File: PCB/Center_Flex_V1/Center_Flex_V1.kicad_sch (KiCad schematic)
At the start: 57 parts, among them J1 Conn_01x02_Pin, J10 Conn_01x02_Socket, J11 Conn_01x02_Pin, J12 Conn_01x02_Socket, J13 Conn_01x02_Socket, J14 Conn_01x02_Pin, J15 Conn_01x02_Pin, J16 Conn_01x02_Socket, J17 Conn_01x02_Socket, J18 Conn_01x02_Pin, J19 Conn_01x02_Pin, J2 Conn_01x02_Socket, J20 Conn_01x02_Socket, J21 Conn_01x02_Pin, J22 Conn_01x02_Socket, J23 Conn_01x02_Socket, J24 Conn_01x02_Pin, J25 Conn_01x02_Pin, J26 Conn_01x02_Socket, J27 Conn_01x02_Socket, J28 Conn_01x02_Pin, J29 Conn_01x02_Pin, J3 Conn_01x02_Socket, J30 Conn_01x02_Socket, J31 Conn_01x02_Pin, J32 Conn_01x02_Socket, J33 Conn_01x02_Socket, J34 Conn_01x02_Pin, J35 Conn_01x02_Pin, J36 Conn_01x02_Socket, J37 Conn_01x02_Socket, J38 Conn_01x02_Pin, J39 Conn_01x02_Pin, J4 Conn_01x02_Pin, J40 Conn_01x02_Socket, J5 Conn_01x02_Pin, J6 Conn_01x02_Socket, J7 Conn_01x02_Socket, J8 Conn_01x02_Pin, J9 Conn_01x02_Pin

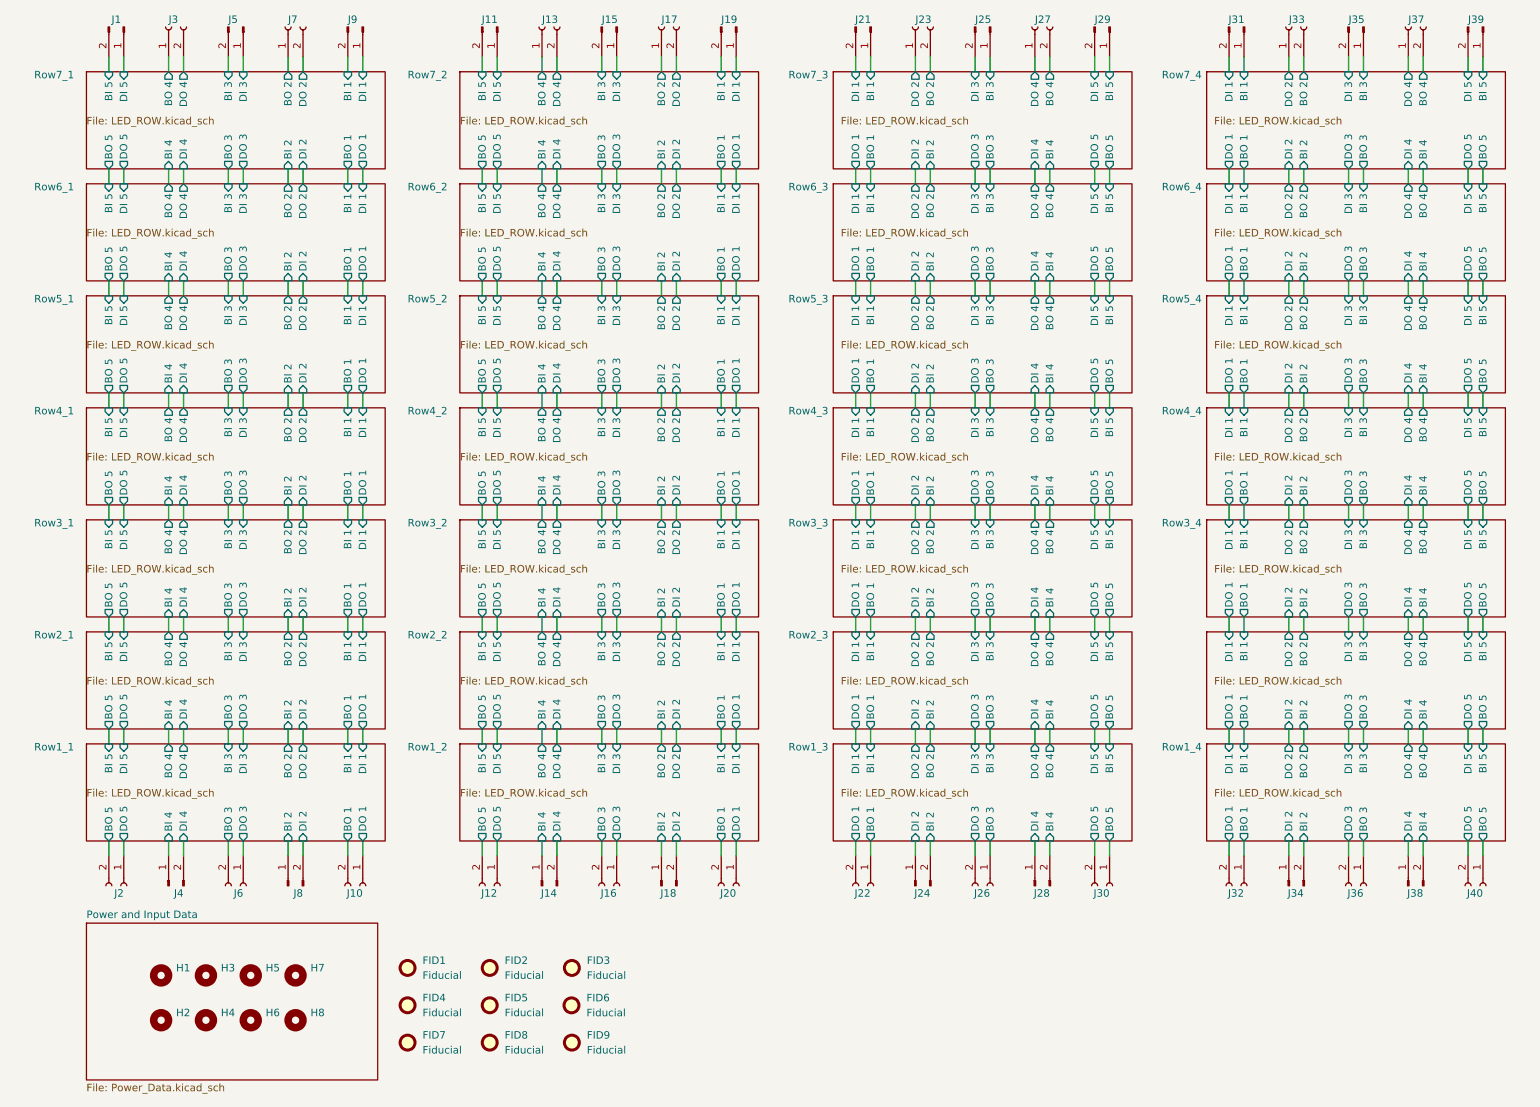
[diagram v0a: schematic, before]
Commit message: Flex PCBs ordered
All Flex PCBs are finalized and ordered
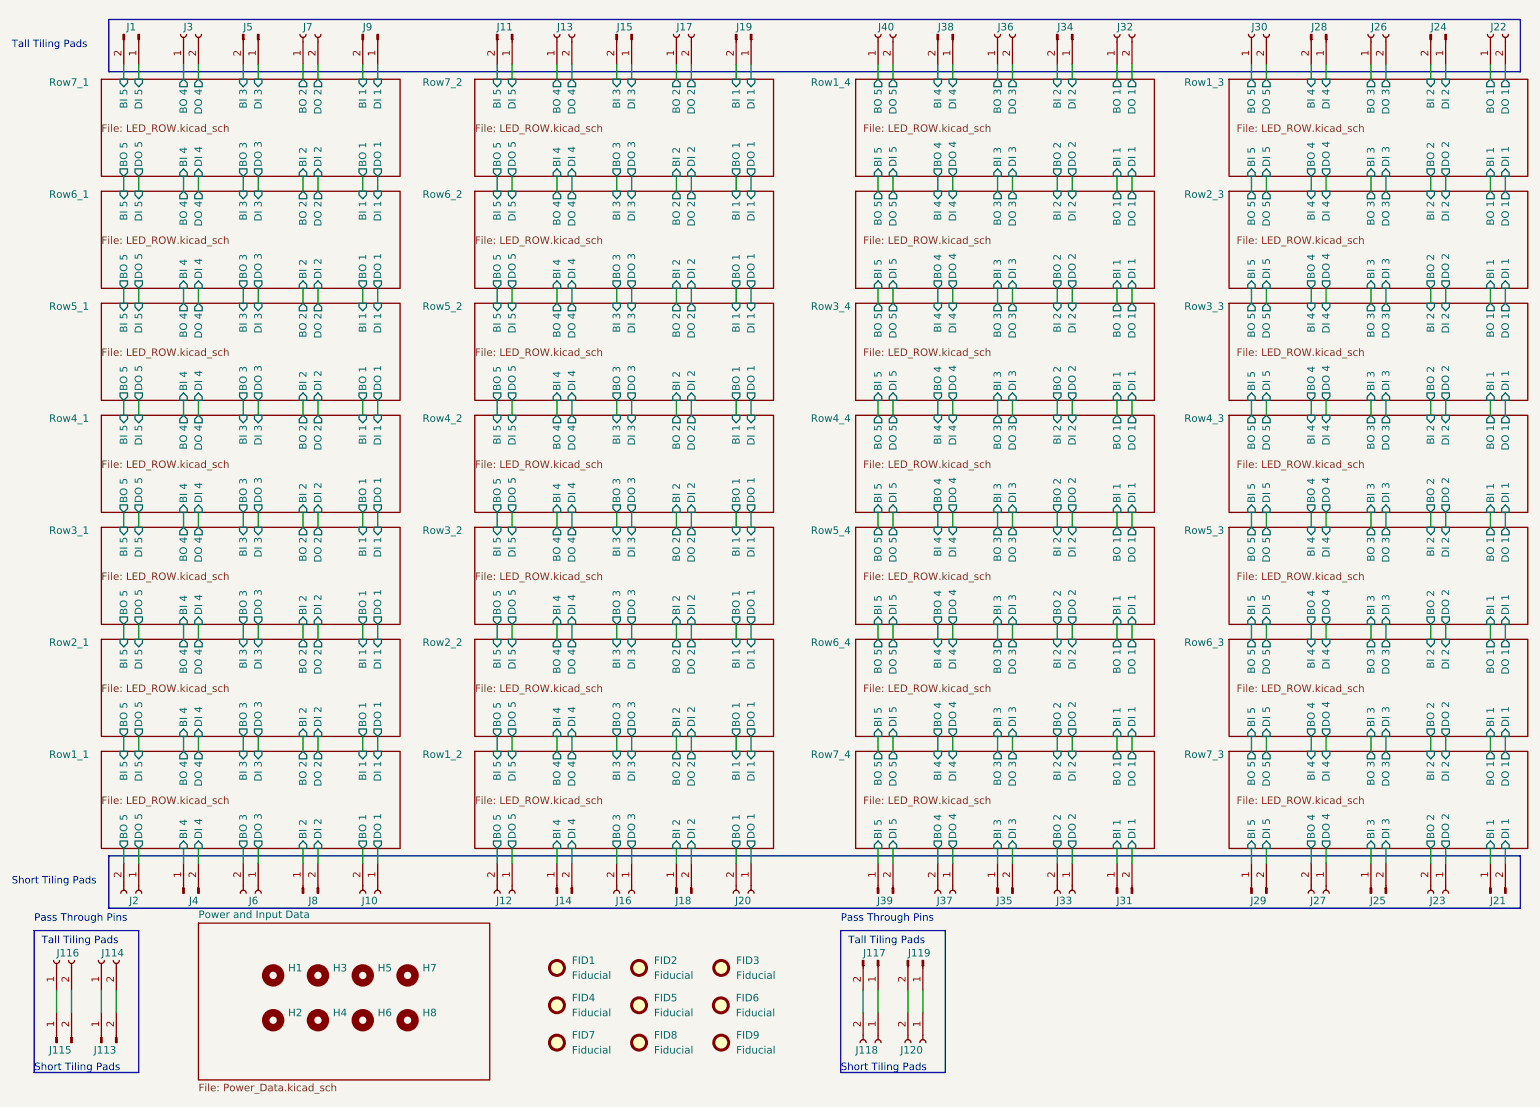
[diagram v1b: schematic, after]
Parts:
- added J113, J115: Conn_01x02_Pin, Dustins_Footprints:Snowboard_Flex_Solder_pad_short, symbol Connector:Conn_01x02_Pin
- added J114, J116: Conn_01x02_Socket, Dustins_Footprints:Snowboard_Flex_Solder_Pad, symbol Connector:Conn_01x02_Socket
- added J117, J119: Conn_01x02_Pin, Dustins_Footprints:Snowboard_Flex_Solder_Pad, symbol Connector:Conn_01x02_Pin
- added J118, J120: Conn_01x02_Socket, Dustins_Footprints:Snowboard_Flex_Solder_pad_short, symbol Connector:Conn_01x02_Socket
- J10, J12, J14, J16, J18, J2, J20, J21, J23, J25, J27, J29, J31, J33, J35, J37, J39, J4, J6, J8: footprint Dustins_Footprints:Snowboard_Flex_Solder_Pad -> Dustins_Footprints:Snowboard_Flex_Solder_pad_short
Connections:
- new net: J117.1 (Pin_1), J118.1 (Pin_1)
- new net: J117.2 (Pin_2), J118.2 (Pin_2)
- new net: J119.1 (Pin_1), J120.1 (Pin_1)
- new net: J119.2 (Pin_2), J120.2 (Pin_2)
- new net: J115.1 (Pin_1), J116.1 (Pin_1)
- new net: J115.2 (Pin_2), J116.2 (Pin_2)
- new net: J113.1 (Pin_1), J114.1 (Pin_1)
- new net: J113.2 (Pin_2), J114.2 (Pin_2)
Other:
- note added: "Pass Through Pins"
- note added: "Short Tiling Pads"
- note added: "Tall Tiling Pads"
- moved on the sheet: FID1, FID2, FID3, FID4, FID5, FID6, FID7, FID8, FID9, H1, H2, H3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
